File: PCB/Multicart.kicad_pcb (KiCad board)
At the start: 2 copper layers, 78 x 89.5 mm, 46 parts, among them J1 MODULE, SW1 BACK, SW2 NEXT, U1 74HC00, U2 74LS573, U3 SST39SF040, U4 SST39SF040, U5 SST39SF040, U6 SA39-11SRWA, U7 MAX810, U8 AT89C2051-12P, Y1 3.6864MHz

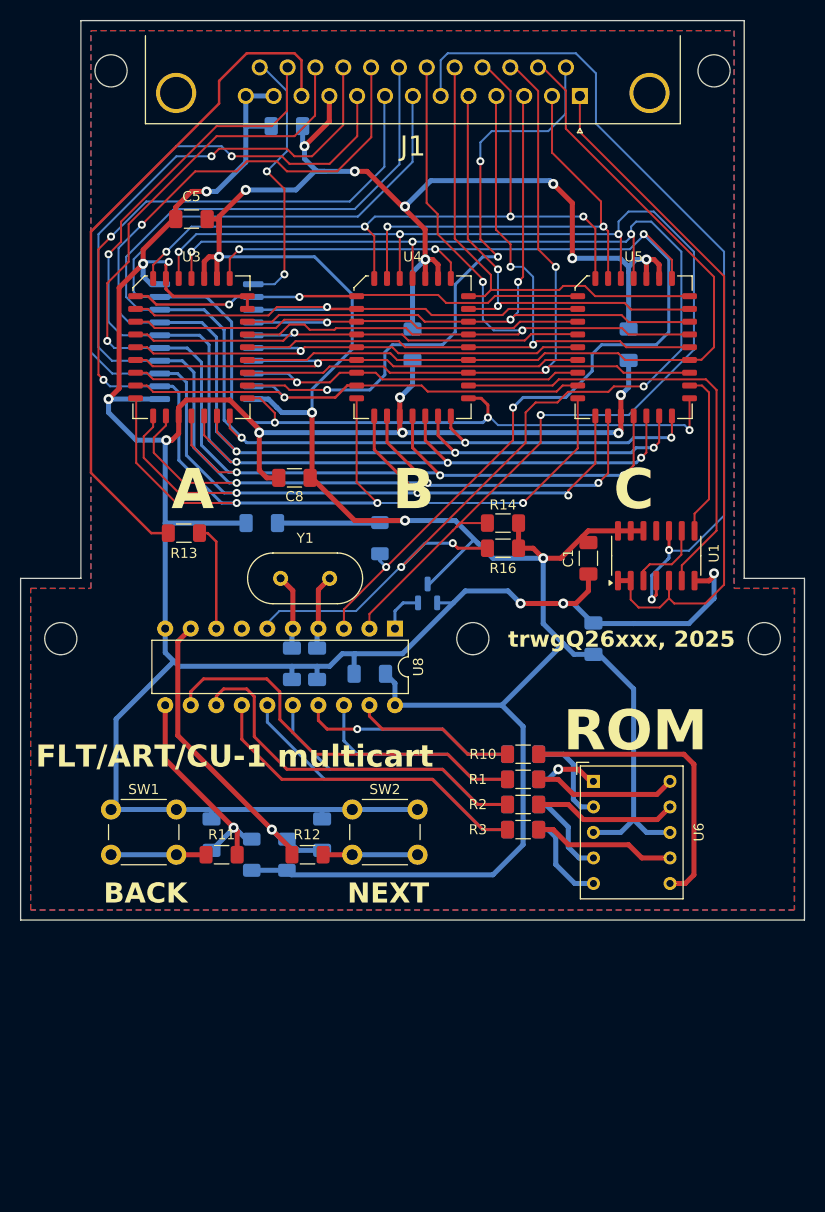
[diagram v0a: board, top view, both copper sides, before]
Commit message: MCU changed to Attiny 406/806, PCB updated to revision C
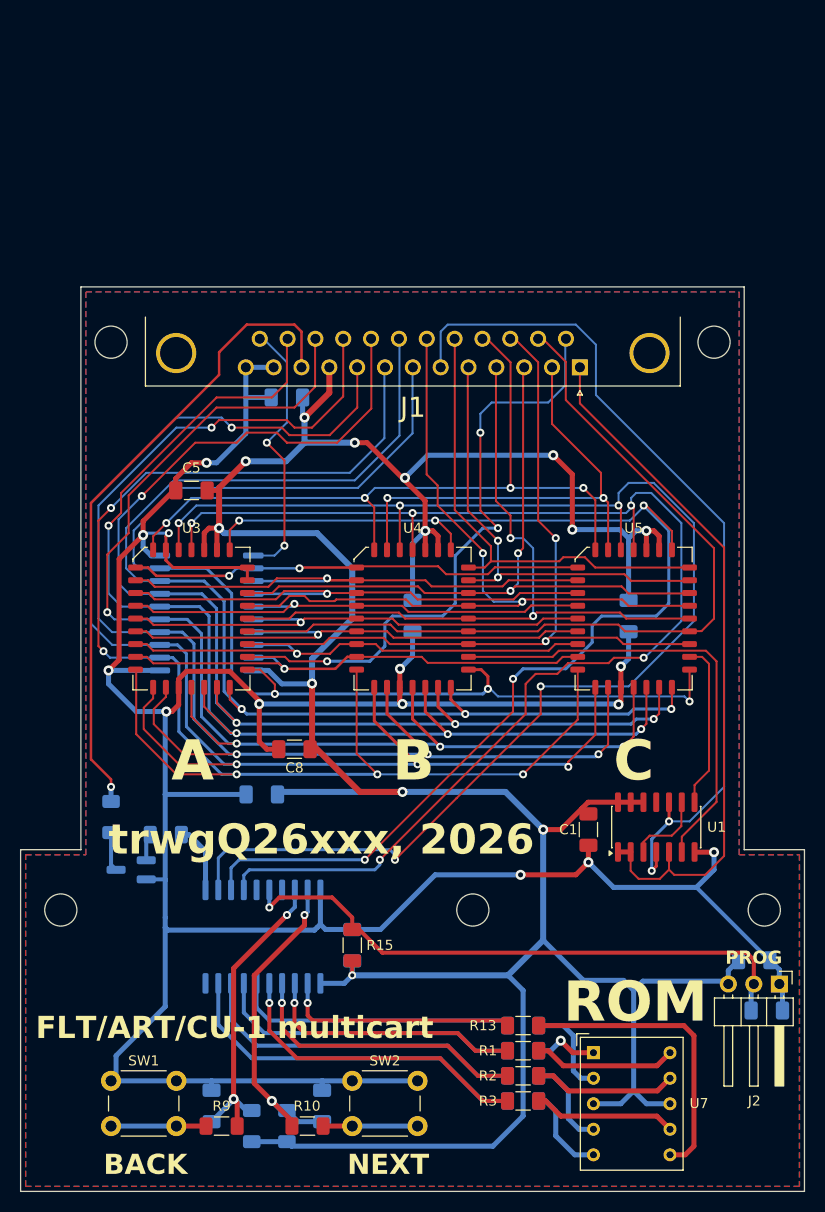
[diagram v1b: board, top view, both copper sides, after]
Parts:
- removed the C10 at (145.5, 84.5)
- removed the C11 at (143.0, 84.5)
- removed R16: 10k, Resistor_SMD:R_1206_3216Metric_Pad1.30x1.75mm_HandSolder
- removed the U7 at (156.5, 77.5)
- removed U8: AT89C2051-12P, Package_DIP:DIP-20_W7.62mm
- removed Y1: 3.6864MHz, Crystal:Crystal_HC49-4H_Vertical
- added C12: DNP, Capacitor_SMD:C_1206_3216Metric_Pad1.33x1.80mm_HandSolder, B.Cu at (190.2, 119.0)
- added J2: PROG, Connector_PinHeader_2.54mm:PinHeader_1x03_P2.54mm_Horizontal, F.Cu at (191.5, 116.4)
- added Q1: BC817, Package_TO_SOT_SMD:SOT-23_Handsoldering, B.Cu at (127.0, 105.0)
- added U6: ATtiny806-S, Package_SO:SOIC-20W_7.5x12.8mm_P1.27mm, B.Cu at (140.1, 111.7)
- J1: footprint Connector_Dsub:DSUB-25_Male_Horizontal_P2.77x2.84mm_EdgePinOffset4.94mm_Housed_MountingHolesOffset7.48mm -> Connector_Dsub:DSUB-25_Pins_Horizontal_P2.77x2.84mm_EdgePinOffset7.70mm_Housed_MountingHolesOffset9.12mm
- R11: renamed from R13; moved to B.Cu
- R14: value 10k -> 4k7; moved to B.Cu
- R15: value 10k -> DNP; moved to F.Cu
- moved R14 45.7 mm to (130.4, 101.5), turned to 180 degrees
- moved R15 40.6 mm to (149.0, 112.5), turned to -90 degrees
- moved C4 35.8 mm to (189.0, 114.0), turned to 0 degrees
- moved R11 29.2 mm to (125.0, 99.8), turned to -90 degrees
- moved C9 27.1 mm to (149.0, 112.5), turned to 90 degrees
- moved C1 27.0 mm to (172.5, 101.0)
- moved C10 27.0 mm to (135.0, 128.5)
- moved C11 27.0 mm to (146.0, 128.5)
- moved C2 27.0 mm to (142.5, 58.0)
- moved C3 27.0 mm to (140.0, 97.5)
- moved C5 27.0 mm to (133.0, 67.2)
- moved C6 27.0 mm to (176.5, 79.8)
- moved C7 27.0 mm to (155.0, 79.8)
- moved C8 27.0 mm to (143.2, 93.0)
- moved H1 27.0 mm to (125.0, 52.5)
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- renumbered C12 to C10, C13 to C11, R12 to R10, R9 to R12, R10 to R13, R6 to R4, R7 to R5, R4 to R6, R5 to R7, R11 to R9, U6 to U7
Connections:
- R1 pad 1: Net-(U8-P1.0) -> LED_A
- R12 pad 1: Net-(U8-P1.6) -> LED_G
- R13 pad 1: Net-(U8-P1.7) -> LED_DP
- R14 pad 1: A16 -> FLT_RST
- R14 pad 2: +5V -> Net-(Q1-B)
- R15 pad 1: A17 -> #CPU_RST
- R2 pad 1: Net-(U8-P1.1) -> LED_B
- R3 pad 1: Net-(U8-P1.2) -> LED_C
- R6 pad 1: Net-(U8-P1.3) -> LED_D
- R7 pad 1: Net-(U8-P1.4) -> LED_E
- R8 pad 1: Net-(U8-P1.5) -> LED_F
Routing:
- net #CPU_RST: track 0.00 -> 59.3 mm, vias 0 -> 1
- net Net-(U8-P1.0): track 39.1 -> 0.00 mm
- net Net-(U8-P1.1): track 37.3 -> 0.00 mm
- net LED_D: track 0.00 -> 36.0 mm
- net Net-(U8-P1.2): track 33.6 -> 0.00 mm
- net LED_E: track 0.00 -> 33.5 mm
- net LED_C: track 0.00 -> 31.3 mm, vias 0 -> 1
- net LED_G: track 0.00 -> 30.7 mm
- net Net-(U8-P1.3): track 30.0 -> 0.00 mm
- net LED_B: track 0.00 -> 28.9 mm, vias 0 -> 1
- net LED_F: track 0.00 -> 28.1 mm
- net Net-(U8-P1.4): track 27.0 -> 0.00 mm
- net LED_A: track 0.00 -> 26.3 mm, vias 0 -> 1
- net LED_DP: track 0.00 -> 23.5 mm, vias 0 -> 1
- net Net-(U8-P1.5): track 21.7 -> 0.00 mm, vias 1 -> 0
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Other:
- board size 78 x 89.5 mm -> 78 x 90 mm
- board text added: "PROG"
- board text added: "trwgQ26xxx, 2026"
- board text removed: "trwgQ26xxx, 2025"
